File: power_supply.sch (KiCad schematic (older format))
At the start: 43 parts, among them IC2 TPS62143RGTR, IC7 TLV62065, T520D337M006ATE045 CPOL, U1 LT3958

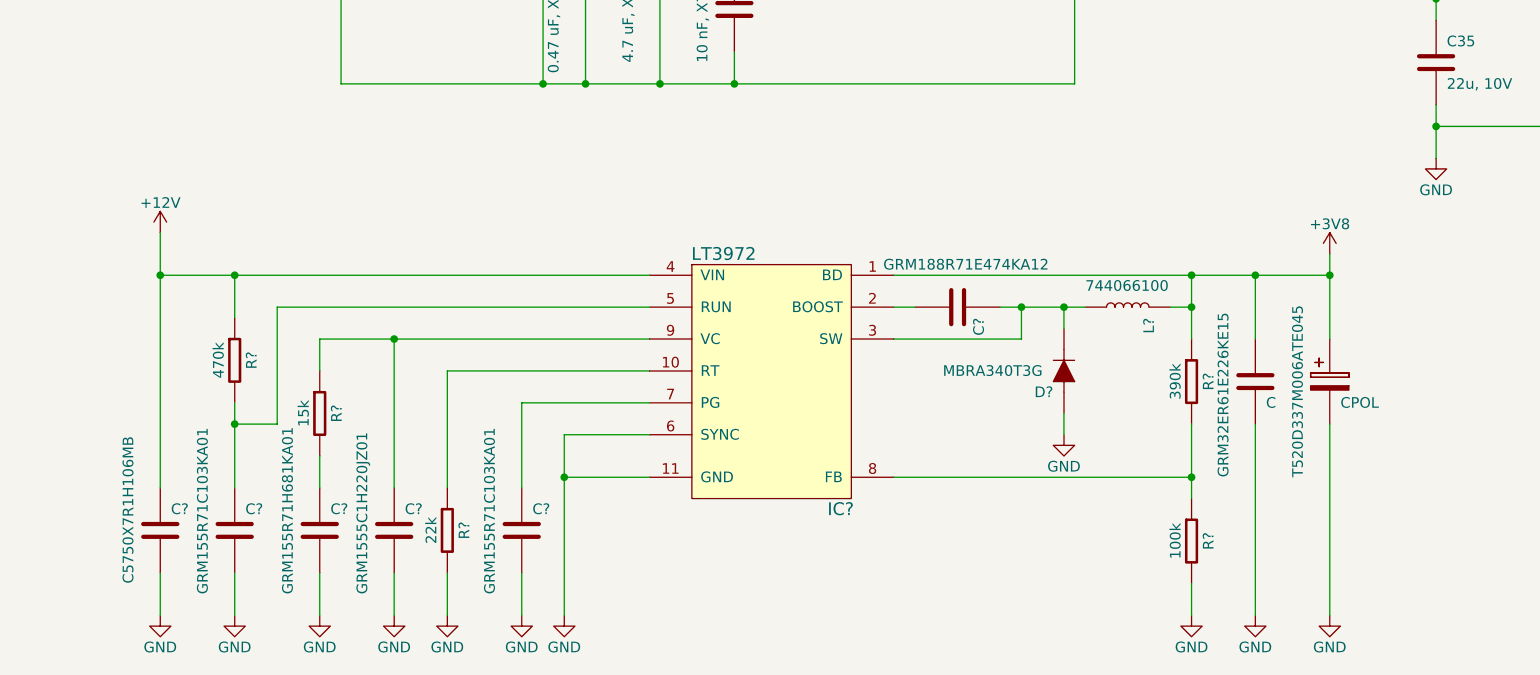
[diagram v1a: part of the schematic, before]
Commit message: 3V8 footprints ergänzt
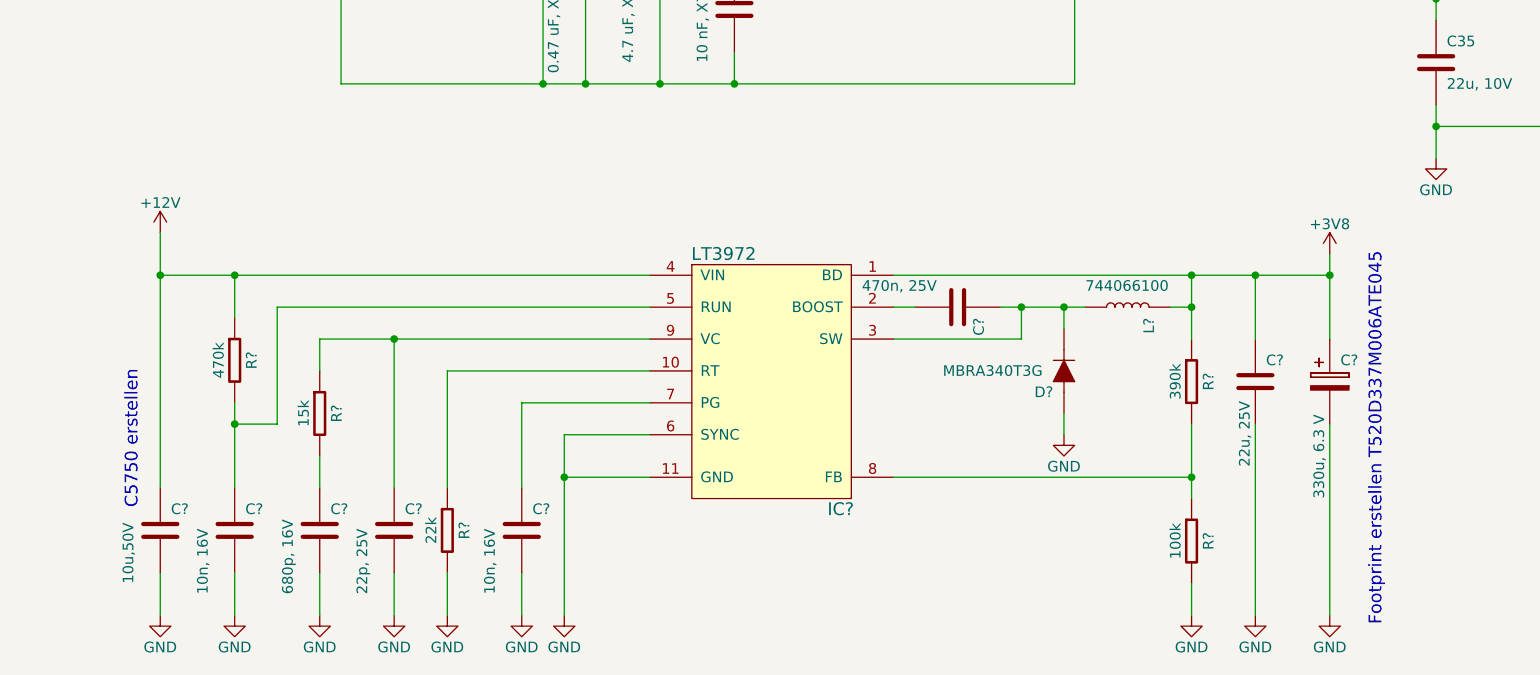
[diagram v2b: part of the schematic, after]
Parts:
- C?: value GRM155R71H681KA01 -> 680p, 16V; footprint (none) -> Passives:C0402N
- C?: value GRM1555C1H220JZ01 -> 22p, 25V; footprint (none) -> Passives:C0402N
- C? (x2): value GRM155R71C103KA01 -> 10n, 16V; footprint (none) -> Passives:C0402N
- C?: value C5750X7R1H106MB -> 10u,50V
- C?: value GRM188R71E474KA12 -> 470n, 25V; footprint (none) -> Passives:C0603N
- C?: renamed from GRM32ER61E226KE15; value C -> 22u, 25V; footprint (none) -> Passives:C1210N
- C?: renamed from T520D337M006ATE045; value CPOL -> 330u, 6.3 V
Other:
- note added: "C5750 erstellen"
- note added: "Footprint erstellen T520D337M006ATE045 \n"
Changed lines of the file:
@@
 P 1900 6700
 F 0 "C?" H 1950 6800 50  0000 L CNN
-F 1 "GRM155R71H681KA01" V 1750 6400 50  0000 L CNN
-F 2 "" H 1938 6550 30  0000 C CNN
-F 3 "" H 1950 6800 60  0000 C CNN
+F 1 "680p, 16V" V 1750 6400 50  0000 L CNN
+F 2 "Passives:C0402N" H 1938 6550 30  0001 C CNN
+F 3 "GRM155R71H681KA01" H 1950 6800 60  0001 C CNN
 	1    1900 6700
 	1    0    0    -1
@@
 P 2250 6700
 F 0 "C?" H 2300 6800 50  0000 L CNN
-F 1 "GRM1555C1H220JZ01" V 2100 6400 50  0000 L CNN
-F 2 "" H 2288 6550 30  0000 C CNN
-F 3 "" H 2300 6800 60  0000 C CNN
+F 1 "22p, 25V" V 2100 6400 50  0000 L CNN
+F 2 "Passives:C0402N" H 2288 6550 30  0001 C CNN
+F 3 "GRM1555C1H220JZ01" H 2300 6800 60  0001 C CNN
 	1    2250 6700
 	1    0    0    -1
@@
 P 2850 6700
 F 0 "C?" H 2900 6800 50  0000 L CNN
-F 1 "GRM155R71C103KA01" V 2700 6400 50  0000 L CNN
-F 2 "" H 2888 6550 30  0000 C CNN
-F 3 "" H 2900 6800 60  0000 C CNN
+F 1 "10n, 16V" V 2700 6400 50  0000 L CNN
+F 2 "Passives:C0402N" H 2888 6550 30  0001 C CNN
+F 3 "GRM155R71C103KA01" H 2900 6800 60  0001 C CNN
 	1    2850 6700
 	1    0    0    -1
@@
 P 1500 6700
 F 0 "C?" H 1550 6800 50  0000 L CNN
-F 1 "GRM155R71C103KA01" V 1350 6400 50  0000 L CNN
-F 2 "" H 1538 6550 30  0000 C CNN
-F 3 "" H 1550 6800 60  0000 C CNN
+F 1 "10n, 16V" V 1350 6400 50  0000 L CNN
+F 2 "Passives:C0402N" H 1538 6550 30  0001 C CNN
+F 3 "GRM155R71C103KA01" H 1550 6800 60  0001 C CNN
 	1    1500 6700
 	1    0    0    -1
@@
 P 1150 6700
 F 0 "C?" H 1200 6800 50  0000 L CNN
-F 1 "C5750X7R1H106MB" V 1000 6450 50  0000 L CNN
+F 1 "10u,50V" V 1000 6450 50  0000 L CNN
 F 2 "" H 1188 6550 30  0000 C CNN
-F 3 "" H 1200 6800 60  0000 C CNN
+F 3 "C5750X7R1H106MB" H 1200 6800 60  0001 C CNN
 	1    1150 6700
 	1    0    0    -1
@@
 P 4900 5650
 F 0 "C?" H 4950 5750 50  0000 L CNN
-F 1 "GRM188R71E474KA12" V 4700 5300 50  0000 L CNN
-F 2 "" H 4938 5500 30  0000 C CNN
-F 3 "" H 4950 5750 60  0000 C CNN
+F 1 "470n, 25V" V 4800 5200 50  0000 L CNN
+F 2 "Passives:C0603N" H 4938 5500 30  0001 C CNN
+F 3 "GRM188R71E474KA12" H 4950 5750 60  0001 C CNN
 	1    4900 5650
 	0    1    1    0
@@
 	5350 850  5750 850
 $Comp
-L C GRM32ER61E226KE15
+L C C?
 U 1 1 5712643C
 P 6300 6000
-F 0 "GRM32ER61E226KE15" V 6150 5550 50  0000 L CNN
-F 1 "C" H 6350 5900 50  0000 L CNN
-F 2 "" H 6338 5850 30  0000 C CNN
-F 3 "" H 6350 6100 60  0000 C CNN
+F 0 "C?" H 6350 6100 50  0000 L CNN
+F 1 "22u, 25V" V 6250 5600 50  0000 L CNN
+F 2 "Passives:C1210N" H 6338 5850 30  0001 C CNN
+F 3 "GRM32ER61E226KE15" H 6350 6100 60  0001 C CNN
 	1    6300 6000
 	1    0    0    -1
 $EndComp
 $Comp
-L CPOL T520D337M006ATE045
+L CPOL C?
 U 1 1 571264E4
 P 6650 6000
-F 0 "T520D337M006ATE045" V 6500 5550 50  0000 L CNN
-F 1 "CPOL" H 6700 5900 50  0000 L CNN
+F 0 "C?" H 6700 6100 50  0000 L CNN
+F 1 "330u, 6.3 V" V 6600 5450 50  0000 L CNN
 F 2 "" H 6688 5850 30  0000 C CNN
-F 3 "" H 6650 6000 60  0000 C CNN
+F 3 "T520D337M006ATE045" H 6650 6000 60  0001 C CNN
 	1    6650 6000
 	1    0    0    -1
@@
 Wire Wire Line
 	6650 6200 6650 7100
+Text Notes 1050 6600 1    60   ~ 0
+C5750 erstellen
+Text Notes 6900 7150 1    60   ~ 0
+Footprint erstellen T520D337M006ATE045 \n
 $EndSCHEMATC

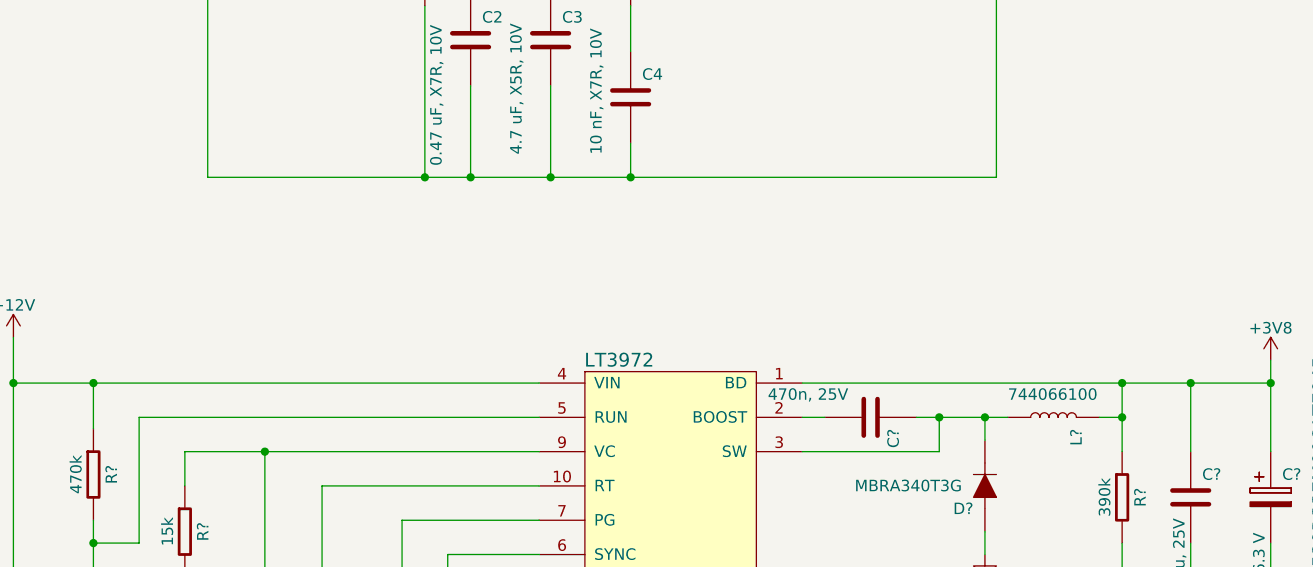
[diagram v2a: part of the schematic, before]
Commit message: NEO N8P durch M8N ersätzt
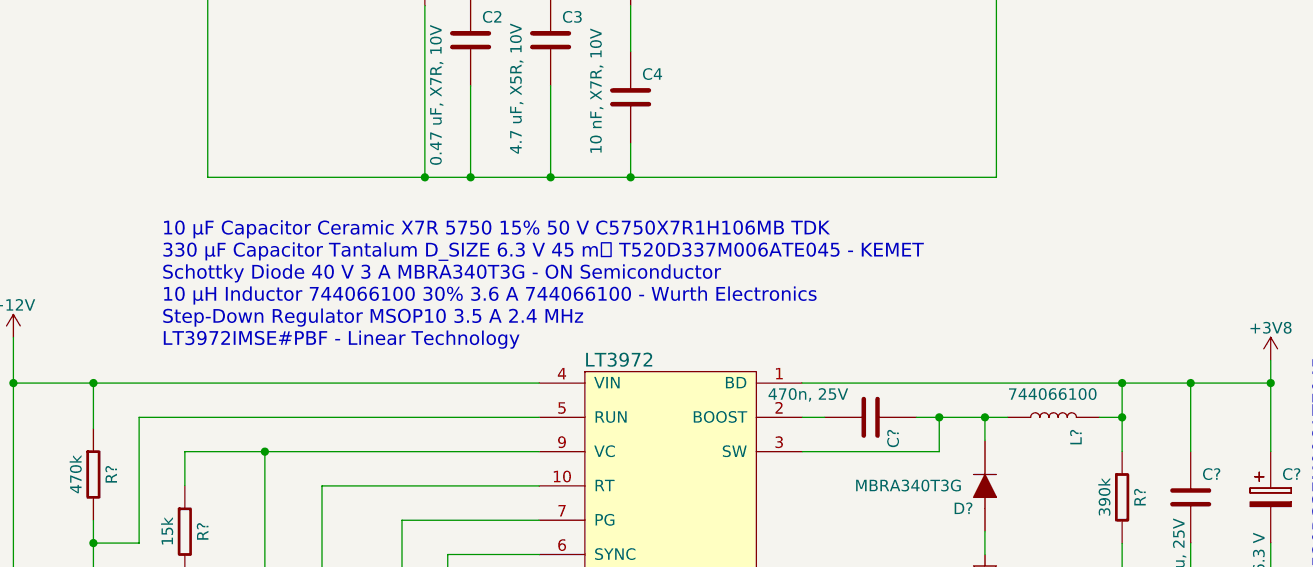
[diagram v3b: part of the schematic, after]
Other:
- note added: "10 μF Capacitor Ceramic X7R 5750 15% 50 V C5750X7R1H106MB TDK \n330 μF Capacitor Tantalum D_SIZE 6.3 V 45 m T520D337M006ATE045 - KEMET \nSchottky Diode 40 V 3 A MBRA340T3G - ON Semiconductor \n10 μH Inductor 744066100 30% 3.6 A 744066100 - Wurth Electronics \nStep-Down Regulator MSOP10 3.5 A 2.4 MHz \nLT3972IMSE#PBF - Linear Technology"

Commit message: footprints ergänzt
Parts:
- D?: footprint (none) -> Passives:D_214_AC
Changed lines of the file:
@@
 F 0 "D?" H 5450 6050 50  0000 L CNN
 F 1 "MBRA340T3G" H 5500 5950 50  0000 L CNN
-F 2 "" H 5438 5800 30  0000 C CNN
+F 2 "Passives:D_214_AC" H 5438 5800 30  0001 C CNN
 F 3 "" H 5400 5950 60  0000 C CNN
 	1    5400 5950

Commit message: added some footprints
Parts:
- IC702: renamed from IC2; footprint (none) -> Switcher_IC:TPS62143
- R702, R705, R710, R711: renamed from R?; footprint (none) -> Passives:R0402N
- gave numbers to parts that had none: 12
- renumbered C2 to C706, C3 to C707, C4 to C708, C5 to C709, C8 to C711, C35 to C714, C9 to C715, C10 to C716, C36 to C717, C11 to C718, C37 to C719, D1 to D701, IC7 to IC703, L1 to L701, L2 to L703, L3 to L704, R1 to R703, R2 to R704, R3 to R706, R4 to R707, R7 to R708, R8 to R709, R29 to R712, R30 to R713, R9 to R714, U1 to U701

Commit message: added footprints
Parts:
- IC701: footprint (none) -> Switcher_IC:DFN_10(3x3)
- L702: footprint (none) -> Passives:744066100
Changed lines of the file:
@@
 F 0 "L702" H 5750 5750 50  0000 L CNN
 F 1 "744066100" V 5600 5450 50  0000 L CNN
-F 2 "" H 5738 5500 30  0001 C CNN
+F 2 "Passives:744066100" H 5738 5500 30  0001 C CNN
 F 3 "" H 5700 5650 60  0000 C CNN
 	1    5700 5650
@@
 F 0 "IC701" H 4350 5500 60  0000 C CNN
 F 1 "LT3972" H 3800 6700 60  0000 C CNN
-F 2 "" H 4050 6100 60  0001 C CNN
+F 2 "Switcher_IC:DFN_10(3x3)" H 4050 6100 60  0001 C CNN
 F 3 "" H 4050 6100 60  0000 C CNN
 	1    4000 6050

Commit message: adjusted power supply
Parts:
- added C720, C721: 10u, 10V, symbol C
- added C722, C723: 22u, 3mOhm, symbol C
- added IC704, IC705: TPS82085, symbol TPS82085
- added R715, R717: 510k, symbol R
- added R716, R718: 162k, symbol R
- added R719, R720: 499k, symbol R
- C713: footprint (none) -> Passives:T520D
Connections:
- net +5V: now also C720.1, C721.1, IC704.1 (EN), IC704.3 (VIN), IC704.4 (VIN), IC705.1 (EN), IC705.3 (VIN), IC705.4 (VIN)
- net GND: now also C720.2, C721.2, C722.2, C723.2, IC704.5 (GND), IC704.6 (GND), IC705.5 (GND), IC705.6 (GND), R716.2, R718.2
- new net: IC705.2 (PG), R720.2
- new net: IC705.7 (FB), R717.2, R718.1
- new net: C723.1, IC705.8 (VOUT), R717.1, R720.1
- new net: IC704.2 (PG), R719.2
- new net: IC704.7 (FB), R715.2, R716.1
- new net: C722.1, IC704.8 (VOUT), R715.1, R719.1
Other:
- note added: "Gibts nicht, 10u 25 C1210 25V???\n"
- note added: "tps82085\n82130\n"
- note removed: "Footprint erstellen T520D337M006ATE045 \n"

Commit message: adjusted power supply and sensors
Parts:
- removed C701: 10u,50V, symbol C
- removed C702, C705: 10n, 16V, Passives:C0402N, symbol C
- removed C703: 680p, 16V, Passives:C0402N, symbol C
- removed C704: 22p, 25V, Passives:C0402N, symbol C
- removed C706: 0.47 uF, X7R, 10V, Passives:C0402N, symbol C
- removed C707: 4.7 uF, X5R, 10V, Passives:C0402N, symbol C
- removed C708: 10 nF, X7R, 10V, Passives:C0402N, symbol C
- removed C709: 2.2 uF, X7R,100V, Passives:C1210N, symbol C
- removed C710: 470n, 25V, Passives:C0603N, symbol C
- removed C711: 22 uF, X5R, 16V, Passives:C1210N, symbol C
- removed C712: 22u, 25V, Passives:C1210N, symbol C
- removed C713: 330u, 6.3 V, Passives:T520D, symbol CPOL
- removed C714, C719: 22u, 10V, Passives:V1206N, symbol C
- removed C715: 10u,25V, Passives:V1210N, symbol C
- removed C716: 3.3n,25V, Passives:C0402N, symbol C
- removed C717: 22p, 10V, Passives:C0402N, symbol C
- removed C718: 47u,6.3V, Passives:C1210N, symbol C
- removed D701: 10MQ100N, Passives:D_SOD124, symbol D
- removed D702: MBRA340T3G, Passives:D_214_AC, symbol D
- removed IC701: LT3972, Switcher_IC:DFN_10(3x3), symbol LT3972
- removed IC702: TPS62143RGTR, Switcher_IC:TPS62143, symbol TPS62143RGTR
- removed IC703: TLV62065, Switcher_IC:TLV62065_WSON, symbol TLV62065
- removed L701: DRQ125, myfootprint:DRQ125, symbol DRQ
- removed L702: 744066100, Passives:744066100, symbol L
- removed L703: 1uH,2A, Passives:L1008N, symbol L
- removed L704: XFL4020-222ME, symbol L
- removed R701: 470k, Passives:V0402N, symbol R
- removed R702: 15k, Passives:R0402N, symbol R
- removed R703: 392k, Passives:R0402N, symbol R
- removed R704: 66.5k, Passives:R0402N, symbol R
- removed R705: 22k, Passives:R0402N, symbol R
- removed R706: 41.2k, Passives:R0402N, symbol R
- removed R707, R708, R709: 10k, Passives:R0402N, symbol R
- removed R710, R712: 390k, Passives:R0402N, symbol R
- removed R711, R714: 100k, Passives:R0402N, symbol R
- removed R713: 86.6k, Passives:R0402N, symbol R
- removed U701: LT3958, myfootprint:UHE28MA, symbol LT3958
- IC704, IC705: footprint (none) -> Switcher_IC:TPS82085
- R715, R716, R718, R719, R720: footprint (none) -> Passives:R0402N
- R717: value 510k -> 649k; footprint (none) -> Passives:R0402N
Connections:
- net +3V3: now also C722.1, IC704.8 (VOUT), R715.1, R719.1
- net +3V8: now also C723.1, IC705.8 (VOUT), R717.1, R720.1
- no-connect marks 5 -> 0
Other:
- note removed: "10 μF Capacitor Ceramic X7R 5750 15% 50 V C5750X7R1H106MB TDK \n330 μF Capacitor Tantalum D_SIZE 6.3 V 45 m T520D337M006ATE045 - KEMET \nSchottky Diode 40 V 3 A MBRA340T3G - ON Semiconductor \n10 μH Inductor 744066100 30% 3.6 A 744066100 - Wurth Electronics \nStep-Down Regulator MSOP10 3.5 A 2.4 MHz \nLT3972IMSE#PBF - Linear Technology"
- note removed: "C5750 erstellen"
- note removed: "Gibts nicht, 10u 25 C1210 25V???\n"
- note removed: "tps82085\n82130\n"
- moved on the sheet: C720, C721, C722, C723, IC704, IC705, R715, R716, R717, R718, R719, R720
